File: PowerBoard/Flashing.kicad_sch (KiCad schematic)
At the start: 32 parts, among them J2 UJ31-CH-G2-SMT-TR, Q1 BSS138, Q4 BSS138, U1 RPI2040, U5 W25Q128JVS, Y1 ABLS-12.000MHZ-B4-T

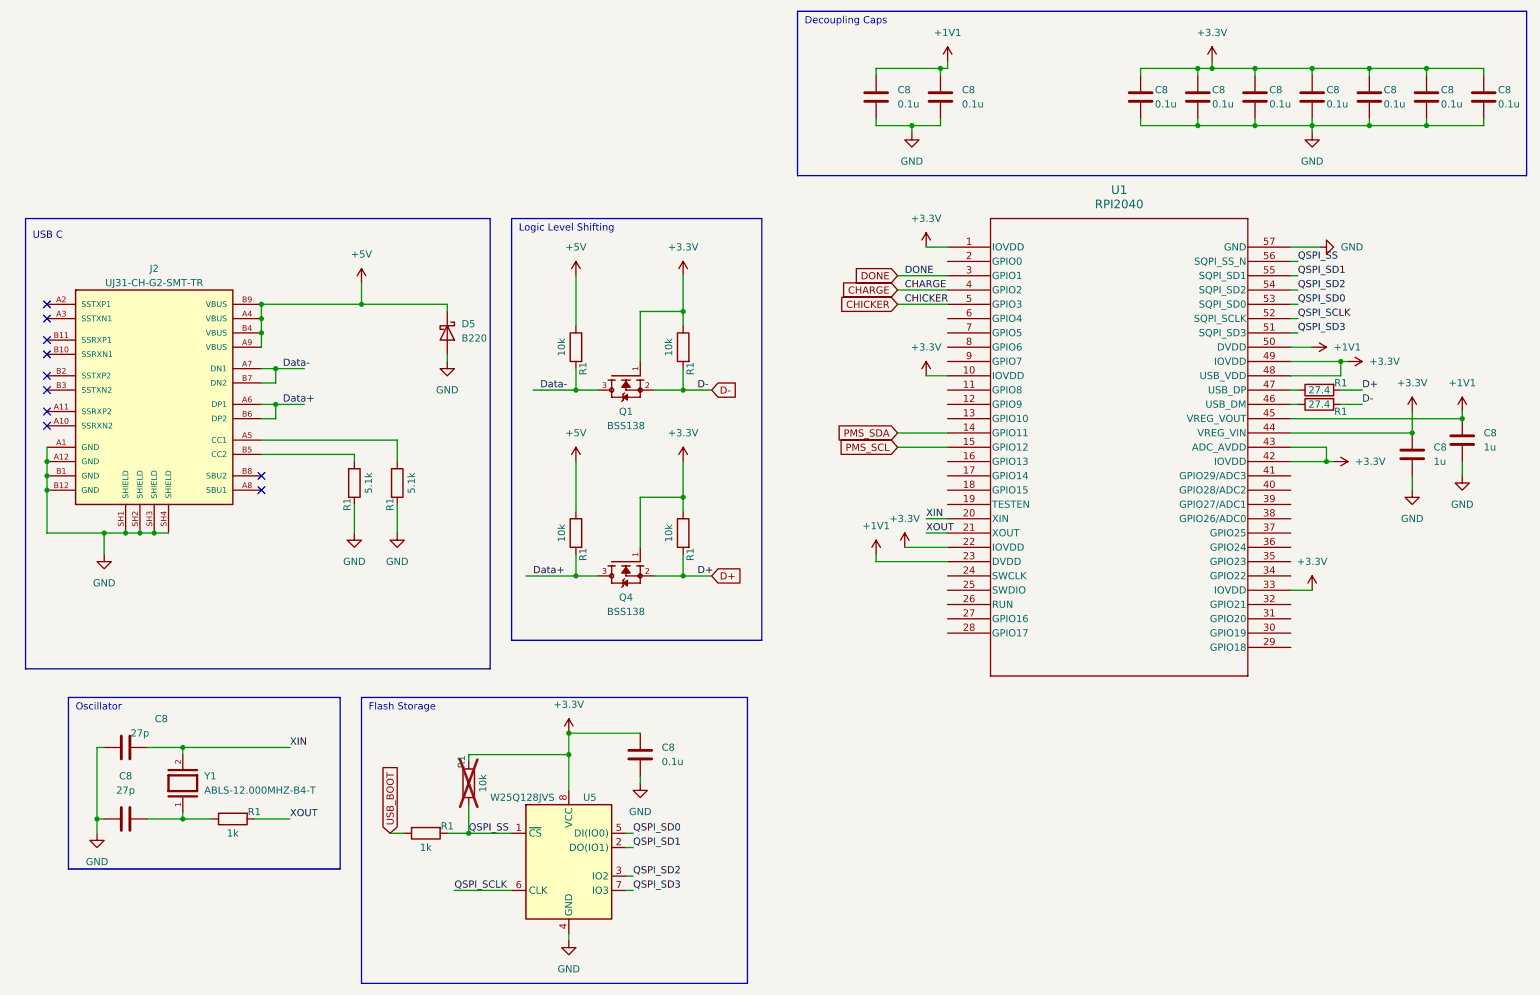
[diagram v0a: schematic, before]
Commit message: updated board shape + placed most components
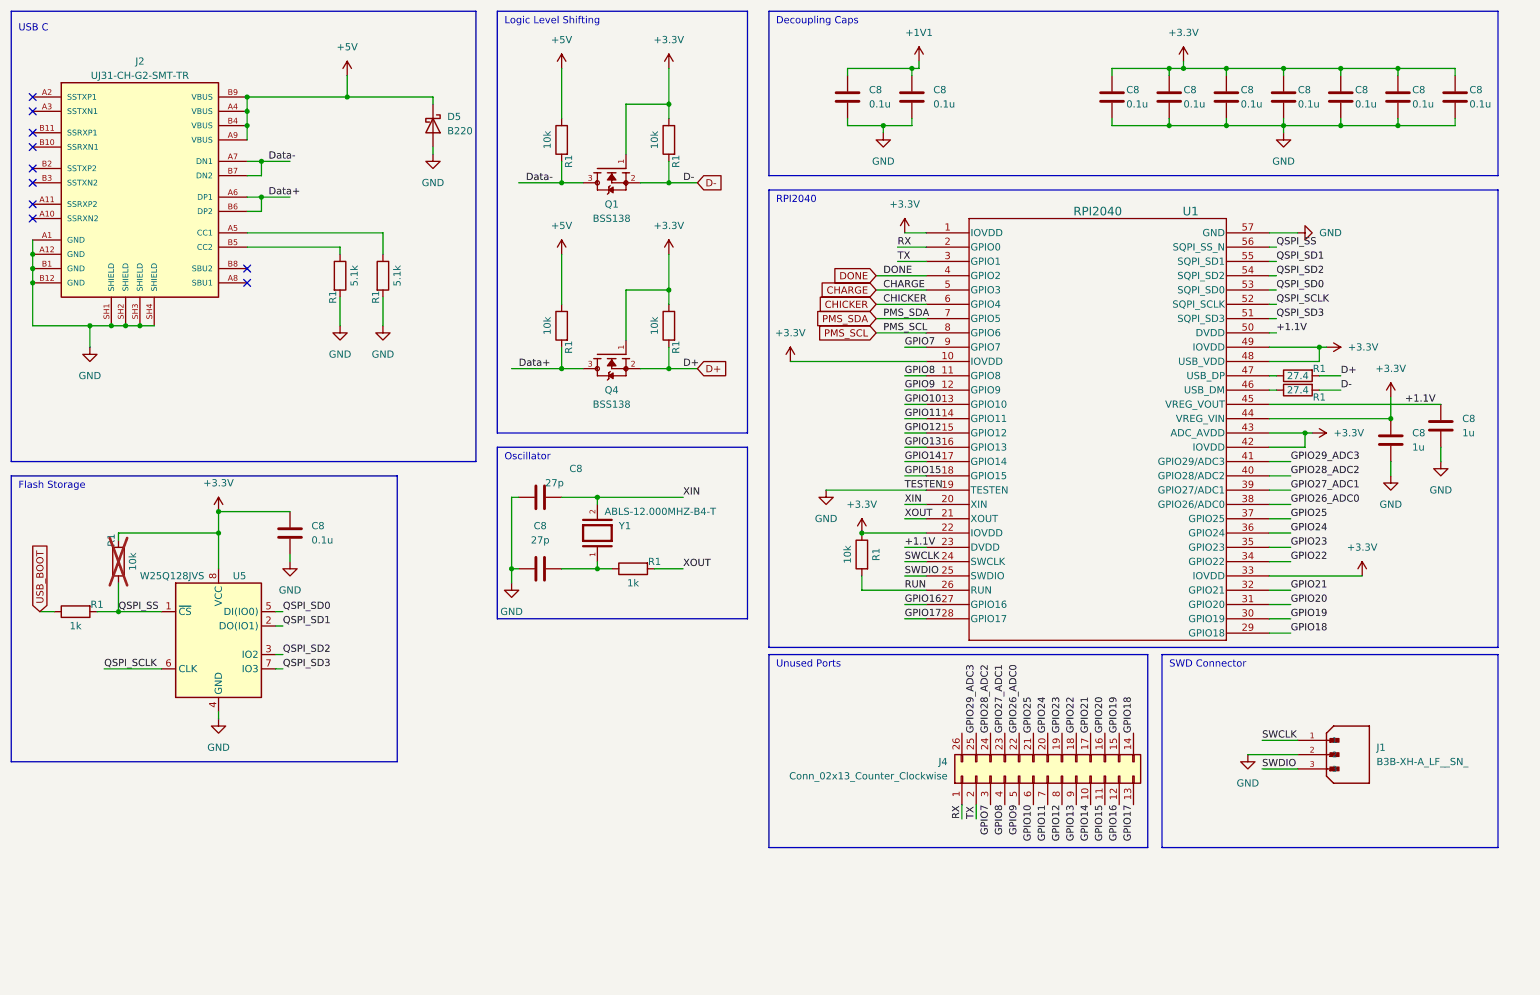
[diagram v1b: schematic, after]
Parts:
- added J1: B3B-XH-A_LF__SN_, B3B-XH-A_LF__SN_:JST_B3B-XH-A_LF__SN_, symbol bots:B3B-XH-A_LF__SN_
- added J4: Conn_02x13_Counter_Clockwise, Connector_PinHeader_2.54mm:PinHeader_2x13_P2.54mm_Vertical, symbol Connector_Generic:Conn_02x13_Counter_Clockwise
- added R1: 10k, Resistor_SMD:R_0603_1608Metric, symbol Device:R
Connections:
- net +1V1: no longer C8.1, U1.23 (DVDD), U1.45 (VREG_VOUT), U1.50 (DVDD)
- net +3.3V: now also R1.1
- net CHARGE: now also U1.5 (GPIO3); no longer U1.4 (GPIO2)
- net CHICKER: now also U1.6 (GPIO4); no longer U1.5 (GPIO3)
- net DONE: now also U1.4 (GPIO2); no longer U1.3 (GPIO1)
- net GND: now also U1.19 (TESTEN), J1.2
- net PMS_SCL: now also U1.8 (GPIO6); no longer U1.15 (GPIO12)
- net PMS_SDA: now also U1.7 (GPIO5); no longer U1.14 (GPIO11)
- net GPIO8: now reaches U1.11 (GPIO8)
- net GPIO8: now also J4.4 (Pin_4)
- net GPIO9: now reaches U1.12 (GPIO9)
- net GPIO9: now also J4.5 (Pin_5)
- net GPIO10: now reaches U1.13 (GPIO10)
- net GPIO10: now also J4.6 (Pin_6)
- net GPIO13: now reaches U1.16 (GPIO13)
- net GPIO13: now also J4.9 (Pin_9)
- net GPIO14: now reaches U1.17 (GPIO14)
- net GPIO14: now also J4.10 (Pin_10)
- net GPIO15: now reaches U1.18 (GPIO15)
- net GPIO15: now also J4.11 (Pin_11)
- net RX: now reaches U1.2 (GPIO0)
- net RX: now also J4.1 (Pin_1)
- net SWCLK: now reaches U1.24 (SWCLK)
- net SWCLK: now also J1.1
- net SWDIO: now reaches U1.25 (SWDIO)
- net SWDIO: now also J1.3
- net RUN: now reaches U1.26 (RUN)
- net RUN: now also R1.2
- net GPIO16: now reaches U1.27 (GPIO16)
- net GPIO16: now also J4.12 (Pin_12)
- net GPIO17: now reaches U1.28 (GPIO17)
- net GPIO17: now also J4.13 (Pin_13)
- net GPIO18: now reaches U1.29 (GPIO18)
- net GPIO18: now also J4.14 (Pin_14)
- net GPIO19: now reaches U1.30 (GPIO19)
- net GPIO19: now also J4.15 (Pin_15)
- net GPIO20: now reaches U1.31 (GPIO20)
- net GPIO20: now also J4.16 (Pin_16)
- net GPIO21: now reaches U1.32 (GPIO21)
- net GPIO21: now also J4.17 (Pin_17)
- net GPIO22: now reaches U1.34 (GPIO22)
- net GPIO22: now also J4.18 (Pin_18)
- net GPIO23: now reaches U1.35 (GPIO23)
- net GPIO23: now also J4.19 (Pin_19)
- net GPIO24: now reaches U1.36 (GPIO24)
- net GPIO24: now also J4.20 (Pin_20)
- net GPIO25: now reaches U1.37 (GPIO25)
- net GPIO25: now also J4.21 (Pin_21)
- net GPIO26_ADC0: now reaches U1.38 (GPIO26/ADC0)
- net GPIO26_ADC0: now also J4.22 (Pin_22)
- net GPIO27_ADC1: now reaches U1.39 (GPIO27/ADC1)
- net GPIO27_ADC1: now also J4.23 (Pin_23)
- net GPIO28_ADC2: now reaches U1.40 (GPIO28/ADC2)
- net GPIO28_ADC2: now also J4.24 (Pin_24)
- net GPIO29_ADC3: now reaches U1.41 (GPIO29/ADC3)
- net GPIO29_ADC3: now also J4.25 (Pin_25)
- net GPIO7: now reaches U1.9 (GPIO7)
- net GPIO7: now also J4.3 (Pin_3)
- new net +1.1V: C8.1, U1.23 (DVDD), U1.45 (VREG_VOUT), U1.50 (DVDD)
- new net GPIO11: J4.7 (Pin_7), U1.14 (GPIO11)
- new net GPIO12: J4.8 (Pin_8), U1.15 (GPIO12)
- new net TX: J4.2 (Pin_2), U1.3 (GPIO1)
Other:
- note added: "RPI2040"
- note added: "SWD Connector"
- note added: "Unused Ports"
- moved on the sheet: C8, D5, J2, Q1, Q4, R1, U1, U5, Y1
